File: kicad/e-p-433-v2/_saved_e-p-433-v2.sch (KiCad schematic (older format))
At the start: 19 parts, among them P3 ant, P5 Transmitter, SW1 Capuchon vert, SW2 SW_PUSH_m, U3 Teensy_3-2

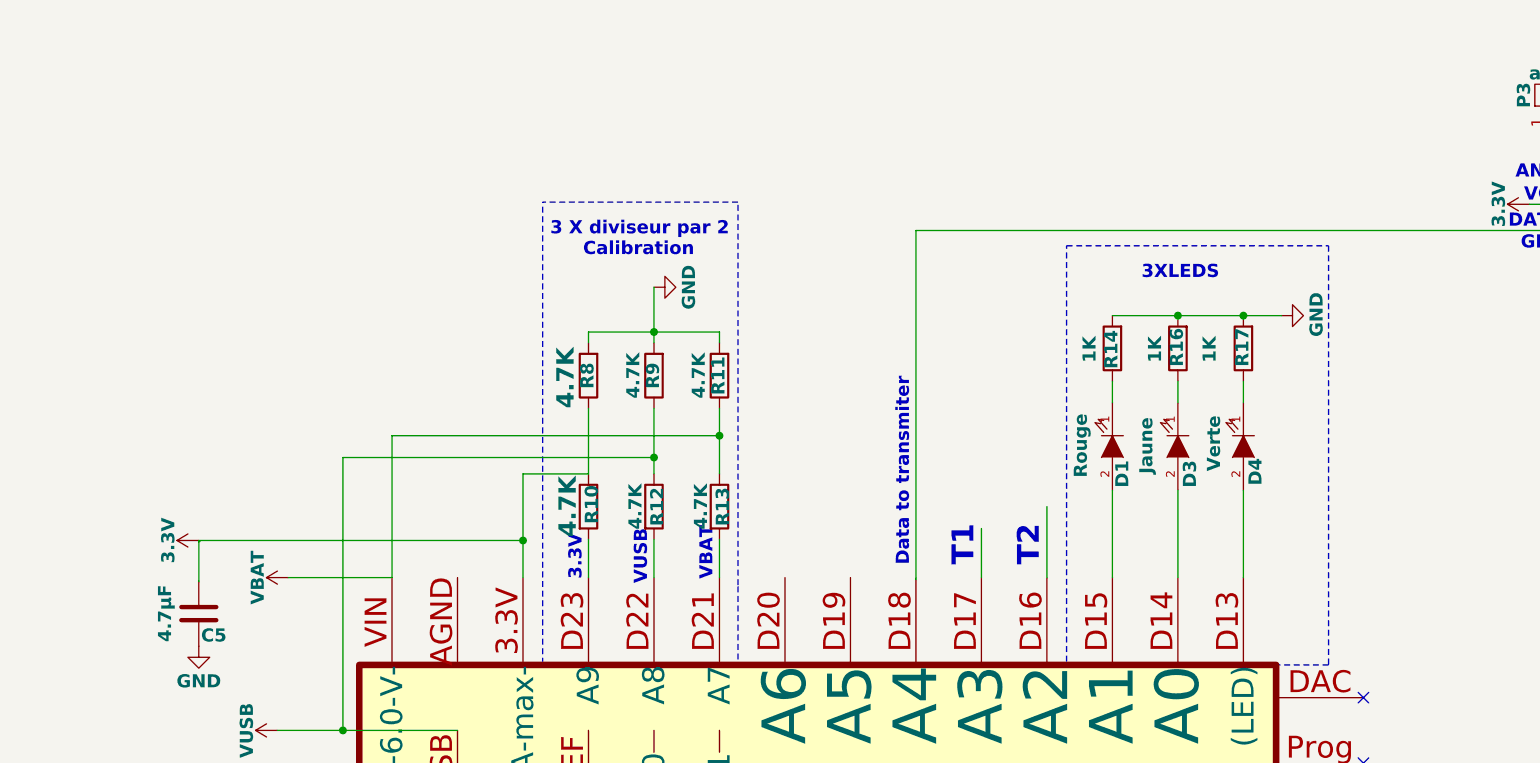
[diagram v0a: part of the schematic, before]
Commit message: Ajout de fichiers et modification de fichiers de la e-p-433-v2
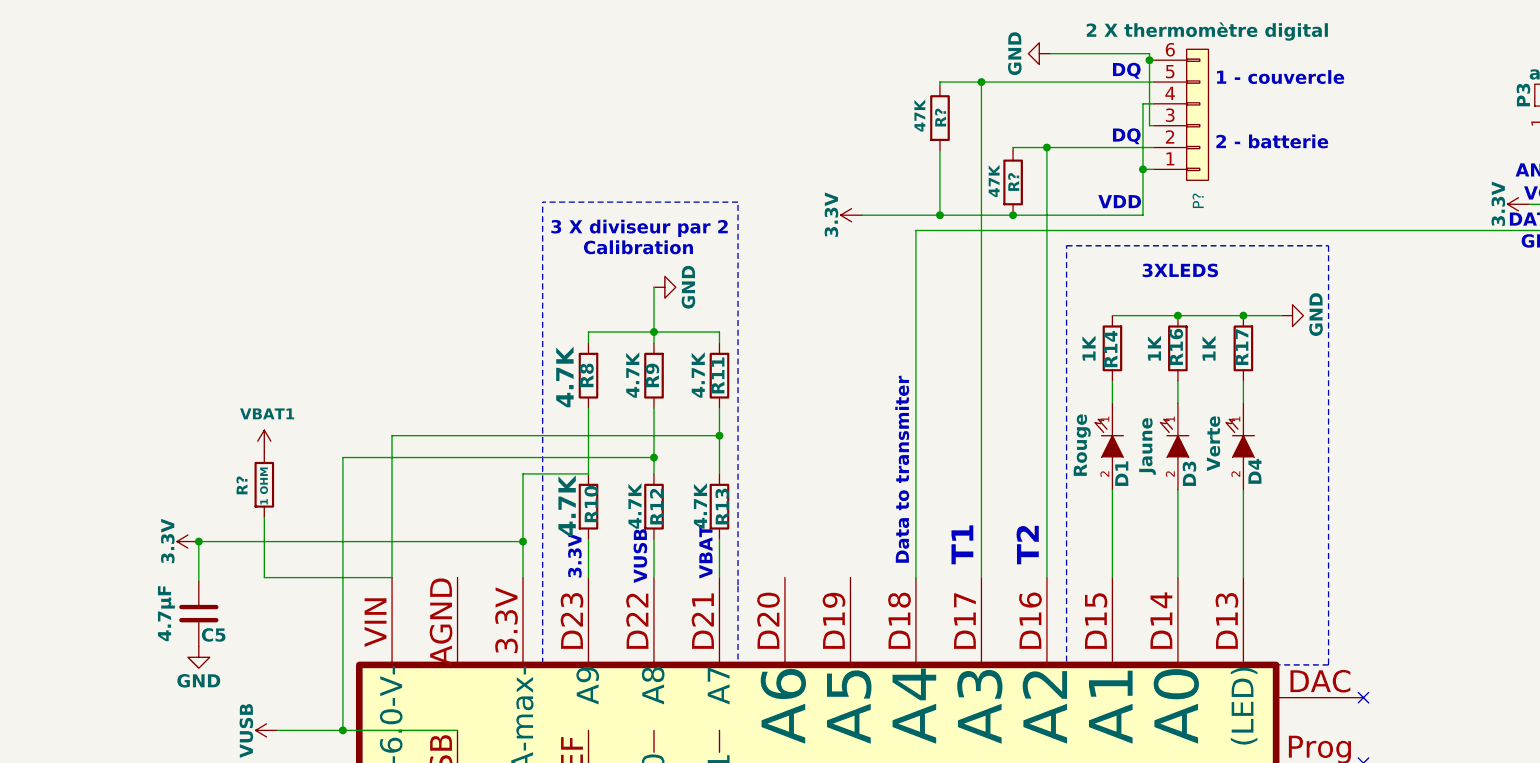
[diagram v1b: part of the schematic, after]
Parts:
- added P?: 2 X thermomètre digital, Connect:PINHEAD1-6, symbol e-p-433-v2-rescue:CONN_01X06
- added R? (x2): 47K, symbol Device:R
- added R?: 1 OHM, symbol Device:R
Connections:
- net labels added: VBAT1
- net labels removed: VBAT
- wire segments 51 -> 70
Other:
- note added: "1 - couvercle"
- note added: "2 - batterie"
- note added: "DQ"
- note added: "VDD"
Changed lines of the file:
@@
-	0    -1   -1   0
-$EndComp
-$Comp
-L Sp:3.3V #PWR13
-U 1 1 582B5D56
-P 3350 2895
-F 0 "#PWR13" H 3350 2745 50  0001 C CNN
-F 1 "3.3V" H 3350 3035 60  0000 C CNB
-F 2 "" H 3350 2895 50  0000 C CNN
-F 3 "" H 3350 2895 50  0000 C CNN
-F 4 "0,00 €" H 3350 2895 60  0001 C CNN "Prix"
-	1    3350 2895
 	0    -1   -1   0
 $EndComp
@@
 	1    3350 3230
 	1    0    0    -1
-$EndComp
-$Comp
-L Sp:VBAT #PWR11
-U 1 1 582CBA63
-P 3760 3065
-F 0 "#PWR11" H 3760 2915 50  0001 C CNN
-F 1 "VBAT" H 3760 3205 60  0000 C CNB
-F 2 "" H 3760 3065 50  0000 C CNN
-F 3 "" H 3760 3065 50  0000 C CNN
-F 4 "0,00 €" H 3760 3065 60  0001 C CNN "Prix"
-	1    3760 3065
-	0    -1   -1   0
 $EndComp
 $Comp
@@
 Connection ~ 8285 5565
 Wire Wire Line
-	6935 3065 6935 2840
-Wire Wire Line
-	7235 2740 7235 3065
-Wire Wire Line
 	4535 3765 4010 3765
 Connection ~ 4010 3765
@@
 	5735 3065 5735 2890
 Wire Wire Line
-	4835 3065 4835 2895
-Wire Wire Line
 	4835 2590 5135 2590
 Wire Wire Line
@@
 	5135 2590 5135 2290
 Connection ~ 5435 2515
-Wire Wire Line
-	4235 3065 3760 3065
 Wire Wire Line
 	4235 3065 4235 2415
@@
 $EndComp
 Wire Wire Line
-	3350 2895 4835 2895
-Connection ~ 4835 2895
-Wire Wire Line
 	6635 3075 6635 1475
 Wire Wire Line
 	6635 1475 9620 1475
 Wire Wire Line
-	3350 3085 3350 2900
-Wire Wire Line
-	3350 2900 3355 2900
-Wire Wire Line
 	8285 5565 8285 5515
 Wire Wire Line
@@
 Wire Wire Line
 	9620 1155 9620 1255
-Wire Wire Line
-	4835 2895 4835 2590
+$Comp
+L e-p-433-v2-rescue:CONN_01X06 P?
+U 1 1 5C3AD164
+P 7925 945
+F 0 "P?" V 7930 1340 50  0000 C CNN
+F 1 "2 X thermomètre digital" H 7970 560 60  0000 C CNB
+F 2 "Connect:PINHEAD1-6" H 7925 945 50  0001 C CNN
+F 3 "https://cdn.sparkfun.com/datasheets/Prototyping/SP-140520-XX-001.pdf" H 7925 945 50  0001 C CNN
+F 4 "Arduino 6-Pin Stackable Headers" H 7925 945 60  0001 C CNN "Désignation"
+F 5 "GCT" H 7925 945 60  0001 C CNN "Fabricant"
+F 6 "SP-140520-06-001" H 7925 945 60  0001 C CNN "Ref-fab"
+F 7 "Sparkfun" H 7925 945 60  0001 C CNN "Distributeur"
+F 8 "PRT09280" H 7925 945 60  0001 C CNN "Ref-distri"
+F 9 "0,50 €" H 7925 945 60  0001 C CNN "Prix"
+	1    7925 945
+	1    0    0    1
+$EndComp
+Wire Wire Line
+	6935 795  7725 795
+Wire Wire Line
+	6935 795  6935 3065
+Wire Wire Line
+	7725 1095 7235 1095
+Wire Wire Line
+	7235 1095 7235 3065
+$Comp
+L Sp:3.3V #PWR13
+U 1 1 582B5D56
+P 3350 2900
+F 0 "#PWR13" H 3350 2750 50  0001 C CNN
+F 1 "3.3V" H 3350 3040 60  0000 C CNB
+F 2 "" H 3350 2900 50  0000 C CNN
+F 3 "" H 3350 2900 50  0000 C CNN
+F 4 "0,00 €" H 3350 2900 60  0001 C CNN "Prix"
+	1    3350 2900
+	0    -1   -1   0
+$EndComp
+Wire Wire Line
+	4835 2590 4835 2900
+Wire Wire Line
+	3350 2900 3350 3080
+Wire Wire Line
+	3350 2900 4835 2900
+Connection ~ 3350 2900
+Connection ~ 4835 2900
+Wire Wire Line
+	4835 2900 4835 3065
+Wire Wire Line
+	7725 995  7705 995
+Wire Wire Line
+	7705 995  7705 695
+Wire Wire Line
+	7705 695  7725 695
+Wire Wire Line
+	7725 895  7675 895
+Wire Wire Line
+	7675 895  7675 1195
+Wire Wire Line
+	7675 1195 7725 1195
+$Comp
+L power:GND #PWR?
+U 1 1 5C3B421C
+P 7250 665
+F 0 "#PWR?" H 7250 415 50  0001 C CNN
+F 1 "GND" H 7250 505 60  0000 C CNB
+F 2 "" H 7250 665 50  0000 C CNN
+F 3 "" H 7250 665 50  0000 C CNN
+	1    7250 665
+	0    1    1    0
+$EndComp
+Wire Wire Line
+	7250 665  7705 665
+Wire Wire Line
+	7705 665  7705 695
+Connection ~ 7705 695
+$Comp
+L Sp:3.3V #PWR?
+U 1 1 5C3B74EB
+P 6390 1405
+F 0 "#PWR?" H 6390 1255 50  0001 C CNN
+F 1 "3.3V" H 6390 1545 60  0000 C CNB
+F 2 "" H 6390 1405 50  0000 C CNN
+F 3 "" H 6390 1405 50  0000 C CNN
+F 4 "0,00 €" H 6390 1405 60  0001 C CNN "Prix"
+	1    6390 1405
+	0    -1   -1   0
+$EndComp
+Connection ~ 7675 1195
+Text Notes 7530 785  0    60   ~ 12
+DQ
+Text Notes 7530 1085 0    60   ~ 12
+DQ
+Text Notes 8005 820  0    60   ~ 12
+1 - couvercle
+Text Notes 8005 1115 0    60   ~ 12
+2 - batterie
+$Comp
+L Device:R R?
+U 1 1 5C3B8EF8
+P 6745 960
+F 0 "R?" V 6750 915 50  0000 L CNB
+F 1 "47K" V 6655 895 50  0000 L CNB
+F 2 "" V 6675 960 50  0001 C CNN
+F 3 "~" H 6745 960 50  0001 C CNN
+	1    6745 960
+	1    0    0    -1
+$EndComp
+Wire Wire Line
+	6935 795  6745 795
+Wire Wire Line
+	6745 795  6745 810
+Connection ~ 6935 795
+$Comp
+L Device:R R?
+U 1 1 5C3BA465
+P 7080 1255
+F 0 "R?" V 7085 1210 50  0000 L CNB
+F 1 "47K" V 6995 1185 50  0000 L CNB
+F 2 "" V 7010 1255 50  0001 C CNN
+F 3 "~" H 7080 1255 50  0001 C CNN
+	1    7080 1255
+	1    0    0    -1
+$EndComp
+Wire Wire Line
+	7235 1095 7080 1095
+Wire Wire Line
+	7080 1095 7080 1105
+Connection ~ 7235 1095
+Wire Wire Line
+	7080 1405 6745 1405
+Wire Wire Line
+	7080 1405 7675 1405
+Wire Wire Line
+	7675 1195 7675 1405
+Connection ~ 7080 1405
+Wire Wire Line
+	6745 1110 6745 1405
+Wire Wire Line
+	6390 1405 6745 1405
+Connection ~ 6745 1405
+Text Notes 7470 1390 0    60   ~ 12
+VDD
+$Comp
+L Sp:VBAT1 #PWR?
+U 1 1 5C3CDFB2
+P 3650 2490
+F 0 "#PWR?" H 3650 2340 50  0001 C CNN
+F 1 "VBAT1" H 3665 2663 50  0000 C CNB
+F 2 "" H 3650 2490 50  0000 C CNN
+F 3 "" H 3650 2490 50  0000 C CNN
+	1    3650 2490
+	1    0    0    -1
+$EndComp
+$Comp
+L Device:R R?
+U 1 1 5C3CF5A6
+P 3650 2640
+F 0 "R?" V 3550 2590 50  0000 L CNB
+F 1 "1 OHM" V 3650 2545 35  0000 L CNB
+F 2 "" V 3580 2640 50  0001 C CNN
+F 3 "~" H 3650 2640 50  0001 C CNN
+	1    3650 2640
+	1    0    0    -1
+$EndComp
+Wire Wire Line
+	3650 2790 3650 3065
+Wire Wire Line
+	3650 3065 4235 3065
 $EndSCHEMATC
